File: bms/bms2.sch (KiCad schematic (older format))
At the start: 19 parts

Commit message: charge shunting and connectors
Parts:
- removed SW?: SW_Push_SPST_NO, footprints:SW_B3U-1000P_4.2x1.7mm, symbol formula:SW_Push_SPST_NO
- added C? (x6): C, symbol Device:C
- added J?: CONN_02X03, footprints:Pin_Header_Straight_2x03, symbol formula:CONN_02X03
- added J?: Conn_01x06_Female, symbol Connector:Conn_01x06_Female
- added Q?: Q_NMOS_SGD, symbol Device:Q_NMOS_SGD
- added Q? (x8): Q_NMOS_DGS, symbol Device:Q_NMOS_DGS
- added R? (x8): R, symbol Device:R
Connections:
- net labels added: +12V, B1, B2, B3, B4, B5, B6, Charge, Discharge, FET1, FET2, FET3, FET4, FET5, FET6, MISO, MOSI, RESET, SCK, VBat, VCC
- wire segments 25 -> 88
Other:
- note added: "Battery Connectors"
- note added: "Buck Power Stage\n"
- note added: "Charge Shuttering"
- note added: "Positive terminals of each battery cell"
- note added: "Power Flags"
- note added: "Programming Header"
- moved on the sheet: C?, D?, L?, Q?, R?, U?A

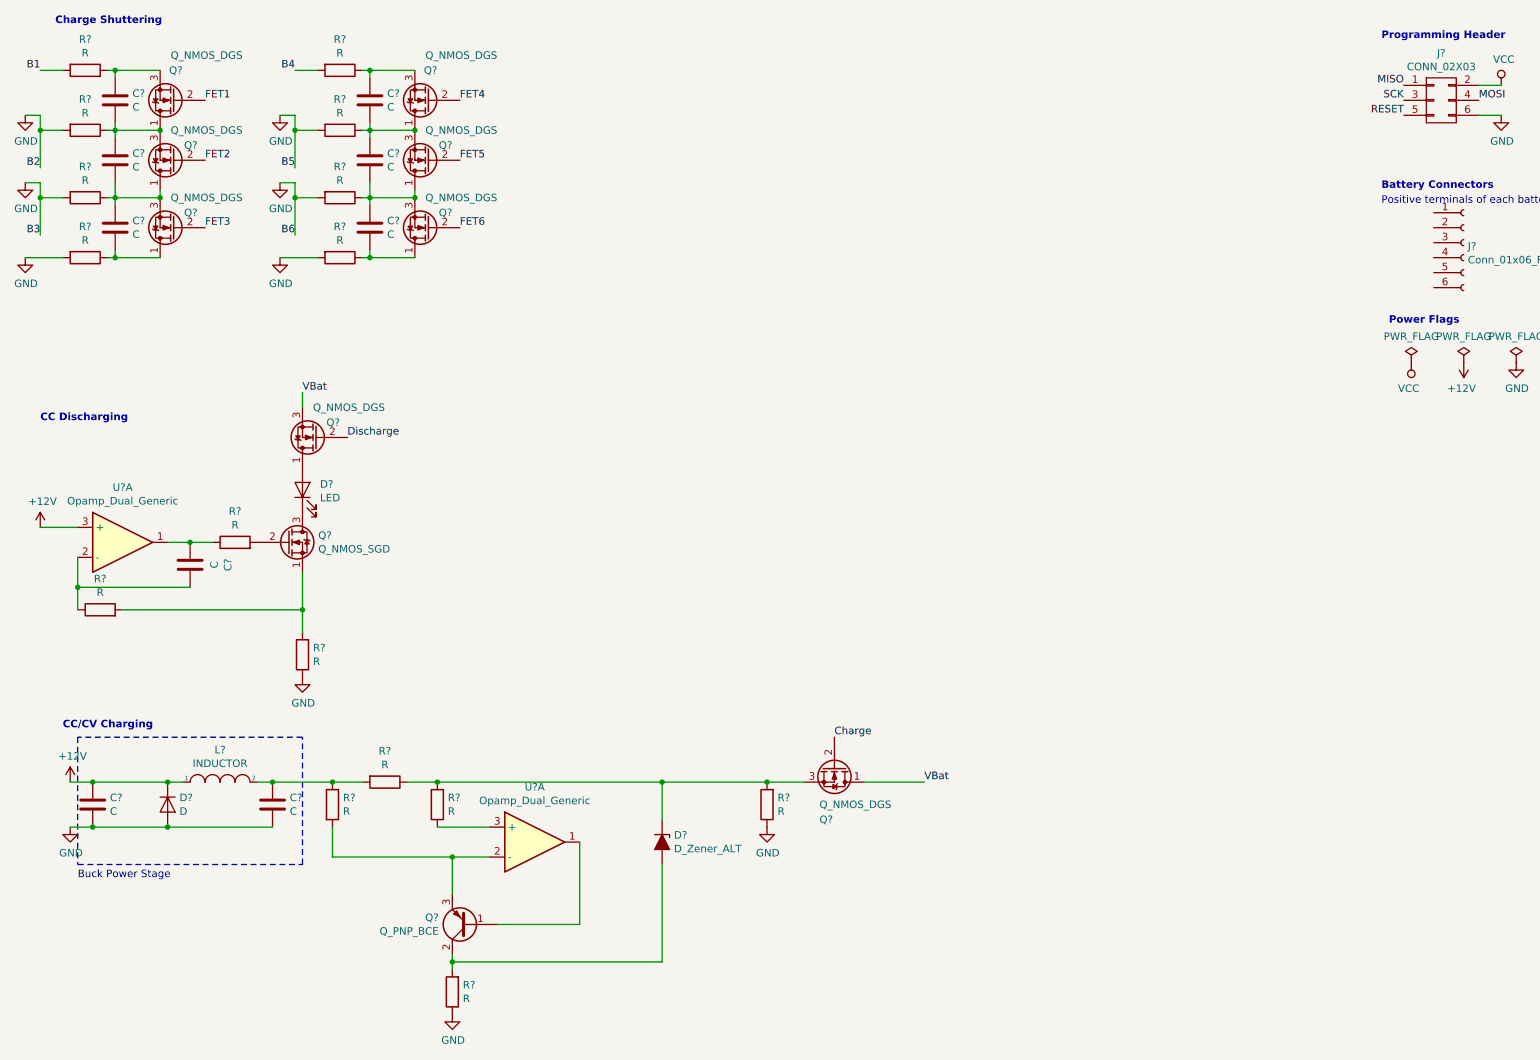
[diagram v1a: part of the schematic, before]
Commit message: integration of connectors, power flags, thermocouples
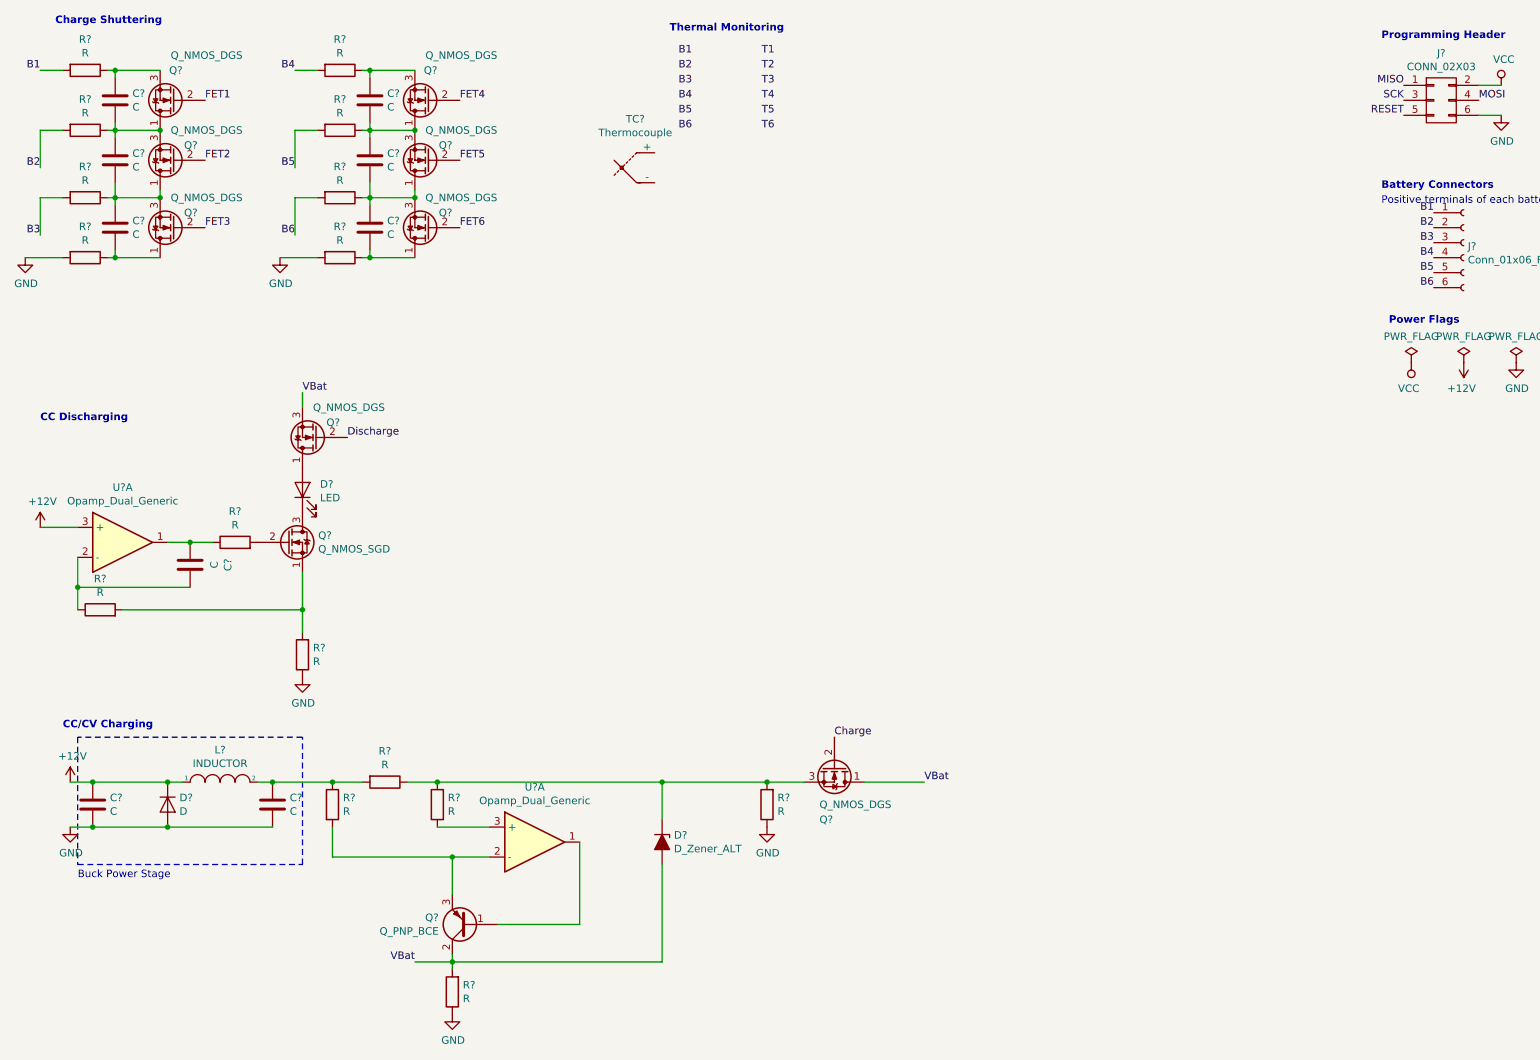
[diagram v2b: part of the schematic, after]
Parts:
- added TC?: Thermocouple, symbol Device:Thermocouple
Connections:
- net B1: now also J?.1 (Pin_1)
- net B4: now also J?.4 (Pin_4)
- net GND: no longer R?.2, R?.2, R?.2, R?.2
- net VBat: now also D?.2 (A), Q?.2 (C), R?.2
- net B2: now reaches J?.2 (Pin_2)
- net B2: now also R?.2
- net B3: now reaches J?.3 (Pin_3)
- net B3: now also R?.2
- net B5: now reaches J?.5 (Pin_5)
- net B5: now also R?.2
- net B6: now reaches J?.6 (Pin_6)
- net B6: now also R?.2
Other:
- note added: "Thermal Monitoring\n"
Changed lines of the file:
@@
 Text Notes 9650 1950 0    50   ~ 0
 Positive terminals of each battery cell
-Wire Wire Line
-	700  1450 700  1350
-Connection ~ 700  1450
-Wire Wire Line
-	700  1900 700  1800
-Connection ~ 700  1900
 Text Label 700  1700 2    50   ~ 0
 B2
 Text Label 700  2150 2    50   ~ 0
 B3
-$Comp
-L power:GND #PWR?
-U 1 1 5E16DCD5
-P 600 1350
-F 0 "#PWR?" H 600 1100 50  0001 C CNN
-F 1 "GND" H 605 1177 50  0000 C CNN
-F 2 "" H 600 1350 50  0001 C CNN
-F 3 "" H 600 1350 50  0001 C CNN
-	1    600  1350
-	1    0    0    -1
-$EndComp
-Wire Wire Line
-	700  1350 600  1350
 Wire Wire Line
 	700  1450 700  1700
-$Comp
-L power:GND #PWR?
-U 1 1 5E170367
-P 600 1800
-F 0 "#PWR?" H 600 1550 50  0001 C CNN
-F 1 "GND" H 605 1627 50  0000 C CNN
-F 2 "" H 600 1800 50  0001 C CNN
-F 3 "" H 600 1800 50  0001 C CNN
-	1    600  1800
-	1    0    0    -1
-$EndComp
-Wire Wire Line
-	700  1800 600  1800
 Wire Wire Line
 	700  1900 700  2150
@@
 Text Label 2400 1050 2    50   ~ 0
 B4
-Wire Wire Line
-	2400 1450 2400 1350
-Connection ~ 2400 1450
-Wire Wire Line
-	2400 1900 2400 1800
-Connection ~ 2400 1900
 Text Label 2400 1700 2    50   ~ 0
 B5
 Text Label 2400 2150 2    50   ~ 0
 B6
-$Comp
-L power:GND #PWR?
-U 1 1 5E177D5A
-P 2300 1350
-F 0 "#PWR?" H 2300 1100 50  0001 C CNN
-F 1 "GND" H 2305 1177 50  0000 C CNN
-F 2 "" H 2300 1350 50  0001 C CNN
-F 3 "" H 2300 1350 50  0001 C CNN
-	1    2300 1350
-	1    0    0    -1
-$EndComp
-Wire Wire Line
-	2400 1350 2300 1350
 Wire Wire Line
 	2400 1450 2400 1700
-$Comp
-L power:GND #PWR?
-U 1 1 5E177D62
-P 2300 1800
-F 0 "#PWR?" H 2300 1550 50  0001 C CNN
-F 1 "GND" H 2305 1627 50  0000 C CNN
-F 2 "" H 2300 1800 50  0001 C CNN
-F 3 "" H 2300 1800 50  0001 C CNN
-	1    2300 1800
-	1    0    0    -1
-$EndComp
-Wire Wire Line
-	2400 1800 2300 1800
 Wire Wire Line
 	2400 1900 2400 2150
@@
 Wire Wire Line
 	6200 5800 6600 5800
+Text Notes 4900 800  0    50   ~ 10
+Thermal Monitoring\n
+Text Label 10000 2000 2    50   ~ 0
+B1
+Text Label 10000 2100 2    50   ~ 0
+B2
+Text Label 10000 2200 2    50   ~ 0
+B3
+Text Label 10000 2300 2    50   ~ 0
+B4
+Text Label 10000 2400 2    50   ~ 0
+B5
+Text Label 10000 2500 2    50   ~ 0
+B6
+Text Label 5050 950  2    50   ~ 0
+B1
+Text Label 5050 1050 2    50   ~ 0
+B2
+Text Label 5050 1150 2    50   ~ 0
+B3
+Text Label 5050 1250 2    50   ~ 0
+B4
+Text Label 5050 1350 2    50   ~ 0
+B5
+Text Label 5050 1450 2    50   ~ 0
+B6
+Text Label 5600 950  2    50   ~ 0
+T1
+Text Label 5600 1050 2    50   ~ 0
+T2
+Text Label 5600 1150 2    50   ~ 0
+T3
+Text Label 5600 1250 2    50   ~ 0
+T4
+Text Label 5600 1350 2    50   ~ 0
+T5
+Text Label 5600 1450 2    50   ~ 0
+T6
+Wire Wire Line
+	3450 7000 3200 7000
+Text Label 3200 7000 2    50   ~ 0
+VBat
+$Comp
+L Device:Thermocouple TC?
+U 1 1 5E196986
+P 4700 1700
+F 0 "TC?" H 4671 2025 50  0000 C CNN
+F 1 "Thermocouple" H 4671 1934 50  0000 C CNN
+F 2 "" H 4125 1750 50  0001 C CNN
+F 3 "~" H 4125 1750 50  0001 C CNN
+	1    4700 1700
+	1    0    0    -1
+$EndComp
 $EndSCHEMATC
